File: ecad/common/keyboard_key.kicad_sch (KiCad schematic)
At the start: 3 parts, among them SW2 SW_Push

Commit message: [WIP] Layouting a matric led driver
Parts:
- D2: renamed from D; footprint (none) -> woodpecker:LED_Inolux_IN-PI32TRRRGB_PLCC4_3.2x2.8mm_P1.5mm; MPN (none) -> IN-P32TRRRGB
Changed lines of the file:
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@@
 		(dnp no)
 		(fields_autoplaced yes)
-		(property "Reference" "D"
+		(property "Reference" "D2"
 			(at 109.22 59.6899 90)
 			(effects
@@
 			)
 		)
-		(property "Footprint" ""
+		(property "Footprint" "woodpecker:LED_Inolux_IN-PI32TRRRGB_PLCC4_3.2x2.8mm_P1.5mm"
 			(at 101.6 60.96 0)
 			(effects
@@
 		(property "Description" "RGB LED, blue/green/red/anode"
 			(at 100.33 60.96 0)
+			(effects
+				(font
+					(size 1.27 1.27)
+				)
+				(hide yes)
+			)
+		)
+		(property "MPN" "IN-P32TRRRGB"
+			(at 100.33 60.96 90)
 			(effects
 				(font
@@
 			(project "top_section"
 				(path "/908c4fb0-9cf3-4739-9176-bc5c47ef8a7b/3e4c3c5e-0959-4abd-bf8c-f1b783d7e681"
-					(reference "D18")
+					(reference "D19")
 					(unit 1)
 				)
 				(path "/908c4fb0-9cf3-4739-9176-bc5c47ef8a7b/47cfd13d-bf73-4a03-a6ca-7b66fdb5bb7d"
-					(reference "D12")
+					(reference "D13")
+					(unit 1)
+				)
+				(path "/908c4fb0-9cf3-4739-9176-bc5c47ef8a7b/61fbcd7b-b588-48a7-b7d7-7589f646c796"
+					(reference "D2")
 					(unit 1)
 				)
 				(path "/908c4fb0-9cf3-4739-9176-bc5c47ef8a7b/6c386fc9-dbbe-48da-a0ca-97d6098257c4"
-					(reference "D20")
+					(reference "D21")
 					(unit 1)
 				)
 				(path "/908c4fb0-9cf3-4739-9176-bc5c47ef8a7b/6c8e40cf-9126-4984-9b5c-e41719a9c800"
-					(reference "D10")
+					(reference "D11")
 					(unit 1)
 				)
 				(path "/908c4fb0-9cf3-4739-9176-bc5c47ef8a7b/72a62481-ec11-41eb-95a3-ab230221a7af"
-					(reference "D22")
+					(reference "D23")
 					(unit 1)
 				)
 				(path "/908c4fb0-9cf3-4739-9176-bc5c47ef8a7b/7f0d18ff-a6af-4cf0-a91c-779951147286"
-					(reference "D24")
+					(reference "D25")
 					(unit 1)
 				)
 				(path "/908c4fb0-9cf3-4739-9176-bc5c47ef8a7b/935564e7-05e7-459d-8b7a-ca61f7462e6f"
-					(reference "D16")
+					(reference "D17")
 					(unit 1)
 				)
 				(path "/908c4fb0-9cf3-4739-9176-bc5c47ef8a7b/b7e74592-5a83-4609-924c-57c795101512"
-					(reference "D14")
+					(reference "D15")
 					(unit 1)
 				)
 				(path "/908c4fb0-9cf3-4739-9176-bc5c47ef8a7b/d85b7b05-f8ab-4186-bcfd-5df52ba17141"
-					(reference "D8")
+					(reference "D9")
 					(unit 1)
 				)
@@
 			(project "top_section"
 				(path "/908c4fb0-9cf3-4739-9176-bc5c47ef8a7b/3e4c3c5e-0959-4abd-bf8c-f1b783d7e681"
-					(reference "D19")
+					(reference "D20")
 					(unit 1)
 				)
 				(path "/908c4fb0-9cf3-4739-9176-bc5c47ef8a7b/47cfd13d-bf73-4a03-a6ca-7b66fdb5bb7d"
-					(reference "D13")
+					(reference "D14")
 					(unit 1)
 				)
@@
 				)
 				(path "/908c4fb0-9cf3-4739-9176-bc5c47ef8a7b/6c386fc9-dbbe-48da-a0ca-97d6098257c4"
-					(reference "D21")
+					(reference "D22")
 					(unit 1)
 				)
 				(path "/908c4fb0-9cf3-4739-9176-bc5c47ef8a7b/6c8e40cf-9126-4984-9b5c-e41719a9c800"
-					(reference "D11")
+					(reference "D12")
 					(unit 1)
 				)
 				(path "/908c4fb0-9cf3-4739-9176-bc5c47ef8a7b/72a62481-ec11-41eb-95a3-ab230221a7af"
-					(reference "D23")
+					(reference "D24")
 					(unit 1)
 				)
 				(path "/908c4fb0-9cf3-4739-9176-bc5c47ef8a7b/7f0d18ff-a6af-4cf0-a91c-779951147286"
-					(reference "D25")
+					(reference "D26")
 					(unit 1)
 				)
 				(path "/908c4fb0-9cf3-4739-9176-bc5c47ef8a7b/935564e7-05e7-459d-8b7a-ca61f7462e6f"
-					(reference "D17")
+					(reference "D18")
 					(unit 1)
 				)
 				(path "/908c4fb0-9cf3-4739-9176-bc5c47ef8a7b/b7e74592-5a83-4609-924c-57c795101512"
-					(reference "D15")
+					(reference "D16")
 					(unit 1)
 				)
 				(path "/908c4fb0-9cf3-4739-9176-bc5c47ef8a7b/d85b7b05-f8ab-4186-bcfd-5df52ba17141"
-					(reference "D9")
-					(unit 1)
-				)
+					(reference "D10")
+					(unit 1)
+				)

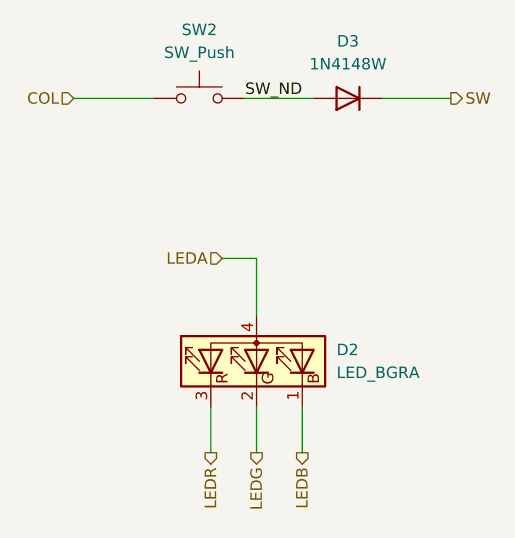
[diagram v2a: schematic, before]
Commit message: Uses LED Matrix controller on all board.
It simplifies so much the design for a small cost.
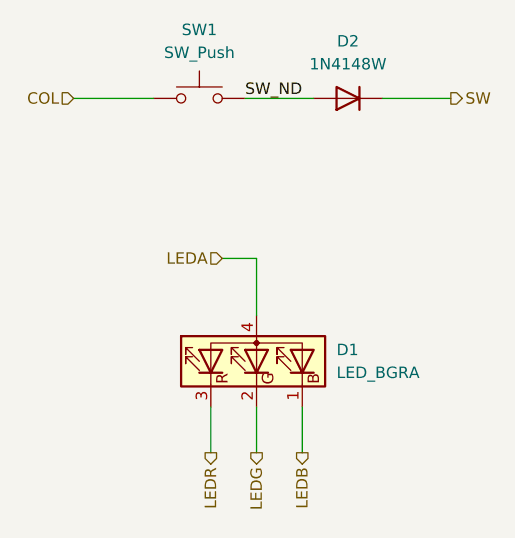
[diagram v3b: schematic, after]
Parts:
- renumbered D2 to D1, D3 to D2, SW2 to SW1
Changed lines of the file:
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@@
 		(on_board yes)
 		(dnp no)
-		(property "Reference" "SW2"
+		(property "Reference" "SW1"
 			(at 93.98 24.13 0)
 			(effects
@@
 		)
 		(instances
-			(project "top_section"
-				(path "/908c4fb0-9cf3-4739-9176-bc5c47ef8a7b/3e4c3c5e-0959-4abd-bf8c-f1b783d7e681"
-					(reference "SW13")
-					(unit 1)
-				)
-				(path "/908c4fb0-9cf3-4739-9176-bc5c47ef8a7b/47cfd13d-bf73-4a03-a6ca-7b66fdb5bb7d"
+			(project "bottom_section"
+				(path "/e5586514-98d8-4785-a096-88fc3a51b1f3/1d252128-5a15-4d61-935a-3deb595aa18f"
+					(reference "SW5")
+					(unit 1)
+				)
+				(path "/e5586514-98d8-4785-a096-88fc3a51b1f3/4e0f2a1f-84c1-4159-b51f-b8ab8493fd2c"
+					(reference "SW6")
+					(unit 1)
+				)
+				(path "/e5586514-98d8-4785-a096-88fc3a51b1f3/5978120e-7110-4ebf-b594-4881798784db"
 					(reference "SW10")
 					(unit 1)
 				)
-				(path "/908c4fb0-9cf3-4739-9176-bc5c47ef8a7b/61fbcd7b-b588-48a7-b7d7-7589f646c796"
+				(path "/e5586514-98d8-4785-a096-88fc3a51b1f3/61a04379-d684-4de2-8564-18b65f6be942"
+					(reference "SW7")
+					(unit 1)
+				)
+				(path "/e5586514-98d8-4785-a096-88fc3a51b1f3/972bcb43-2c03-4a62-ab04-b4b2649c149d"
+					(reference "SW4")
+					(unit 1)
+				)
+				(path "/e5586514-98d8-4785-a096-88fc3a51b1f3/a60112cb-2a25-4cee-b7dc-a72ac75dbb95"
+					(reference "SW9")
+					(unit 1)
+				)
+				(path "/e5586514-98d8-4785-a096-88fc3a51b1f3/b05b7d89-e8e3-4430-b508-1898dbbdfc32"
+					(reference "SW1")
+					(unit 1)
+				)
+				(path "/e5586514-98d8-4785-a096-88fc3a51b1f3/e33e4fdc-bd58-4c67-bb99-1ce8e87238a8"
 					(reference "SW2")
 					(unit 1)
 				)
-				(path "/908c4fb0-9cf3-4739-9176-bc5c47ef8a7b/6c386fc9-dbbe-48da-a0ca-97d6098257c4"
-					(reference "SW14")
-					(unit 1)
-				)
-				(path "/908c4fb0-9cf3-4739-9176-bc5c47ef8a7b/6c8e40cf-9126-4984-9b5c-e41719a9c800"
-					(reference "SW9")
-					(unit 1)
-				)
-				(path "/908c4fb0-9cf3-4739-9176-bc5c47ef8a7b/72a62481-ec11-41eb-95a3-ab230221a7af"
-					(reference "SW15")
-					(unit 1)
-				)
-				(path "/908c4fb0-9cf3-4739-9176-bc5c47ef8a7b/7f0d18ff-a6af-4cf0-a91c-779951147286"
-					(reference "SW16")
-					(unit 1)
-				)
-				(path "/908c4fb0-9cf3-4739-9176-bc5c47ef8a7b/935564e7-05e7-459d-8b7a-ca61f7462e6f"
-					(reference "SW12")
-					(unit 1)
-				)
-				(path "/908c4fb0-9cf3-4739-9176-bc5c47ef8a7b/b7e74592-5a83-4609-924c-57c795101512"
-					(reference "SW11")
-					(unit 1)
-				)
-				(path "/908c4fb0-9cf3-4739-9176-bc5c47ef8a7b/d85b7b05-f8ab-4186-bcfd-5df52ba17141"
+				(path "/e5586514-98d8-4785-a096-88fc3a51b1f3/e46df20f-6acd-4ec4-b154-0a8435b82625"
 					(reference "SW8")
+					(unit 1)
+				)
+				(path "/e5586514-98d8-4785-a096-88fc3a51b1f3/fe8acc3a-547c-469d-9f32-08486ec377e4"
+					(reference "SW3")
 					(unit 1)
 				)
@@
 		(dnp no)
 		(fields_autoplaced yes)
-		(property "Reference" "D2"
+		(property "Reference" "D1"
 			(at 109.22 59.6899 90)
 			(effects
@@
 		)
 		(instances
-			(project "top_section"
-				(path "/908c4fb0-9cf3-4739-9176-bc5c47ef8a7b/3e4c3c5e-0959-4abd-bf8c-f1b783d7e681"
+			(project "bottom_section"
+				(path "/e5586514-98d8-4785-a096-88fc3a51b1f3/1d252128-5a15-4d61-935a-3deb595aa18f"
+					(reference "D9")
+					(unit 1)
+				)
+				(path "/e5586514-98d8-4785-a096-88fc3a51b1f3/4e0f2a1f-84c1-4159-b51f-b8ab8493fd2c"
+					(reference "D11")
+					(unit 1)
+				)
+				(path "/e5586514-98d8-4785-a096-88fc3a51b1f3/5978120e-7110-4ebf-b594-4881798784db"
 					(reference "D19")
 					(unit 1)
 				)
-				(path "/908c4fb0-9cf3-4739-9176-bc5c47ef8a7b/47cfd13d-bf73-4a03-a6ca-7b66fdb5bb7d"
+				(path "/e5586514-98d8-4785-a096-88fc3a51b1f3/61a04379-d684-4de2-8564-18b65f6be942"
 					(reference "D13")
 					(unit 1)
 				)
-				(path "/908c4fb0-9cf3-4739-9176-bc5c47ef8a7b/61fbcd7b-b588-48a7-b7d7-7589f646c796"
-					(reference "D2")
-					(unit 1)
-				)
-				(path "/908c4fb0-9cf3-4739-9176-bc5c47ef8a7b/6c386fc9-dbbe-48da-a0ca-97d6098257c4"
-					(reference "D21")
-					(unit 1)
-				)
-				(path "/908c4fb0-9cf3-4739-9176-bc5c47ef8a7b/6c8e40cf-9126-4984-9b5c-e41719a9c800"
-					(reference "D11")
-					(unit 1)
-				)
-				(path "/908c4fb0-9cf3-4739-9176-bc5c47ef8a7b/72a62481-ec11-41eb-95a3-ab230221a7af"
-					(reference "D23")
-					(unit 1)
-				)
-				(path "/908c4fb0-9cf3-4739-9176-bc5c47ef8a7b/7f0d18ff-a6af-4cf0-a91c-779951147286"
-					(reference "D25")
-					(unit 1)
-				)
-				(path "/908c4fb0-9cf3-4739-9176-bc5c47ef8a7b/935564e7-05e7-459d-8b7a-ca61f7462e6f"
+				(path "/e5586514-98d8-4785-a096-88fc3a51b1f3/972bcb43-2c03-4a62-ab04-b4b2649c149d"
+					(reference "D7")
+					(unit 1)
+				)
+				(path "/e5586514-98d8-4785-a096-88fc3a51b1f3/a60112cb-2a25-4cee-b7dc-a72ac75dbb95"
 					(reference "D17")
 					(unit 1)
 				)
-				(path "/908c4fb0-9cf3-4739-9176-bc5c47ef8a7b/b7e74592-5a83-4609-924c-57c795101512"
+				(path "/e5586514-98d8-4785-a096-88fc3a51b1f3/b05b7d89-e8e3-4430-b508-1898dbbdfc32"
+					(reference "D1")
+					(unit 1)
+				)
+				(path "/e5586514-98d8-4785-a096-88fc3a51b1f3/e33e4fdc-bd58-4c67-bb99-1ce8e87238a8"
+					(reference "D3")
+					(unit 1)
+				)
+				(path "/e5586514-98d8-4785-a096-88fc3a51b1f3/e46df20f-6acd-4ec4-b154-0a8435b82625"
 					(reference "D15")
 					(unit 1)
 				)
-				(path "/908c4fb0-9cf3-4739-9176-bc5c47ef8a7b/d85b7b05-f8ab-4186-bcfd-5df52ba17141"
-					(reference "D9")
+				(path "/e5586514-98d8-4785-a096-88fc3a51b1f3/fe8acc3a-547c-469d-9f32-08486ec377e4"
+					(reference "D5")
 					(unit 1)
 				)
@@
 		(dnp no)
 		(fields_autoplaced yes)
-		(property "Reference" "D3"
+		(property "Reference" "D2"
 			(at 110.49 25.4 0)
 			(effects
@@
 		)
 		(instances
-			(project "top_section"
-				(path "/908c4fb0-9cf3-4739-9176-bc5c47ef8a7b/3e4c3c5e-0959-4abd-bf8c-f1b783d7e681"
+			(project "bottom_section"
+				(path "/e5586514-98d8-4785-a096-88fc3a51b1f3/1d252128-5a15-4d61-935a-3deb595aa18f"
+					(reference "D10")
+					(unit 1)
+				)
+				(path "/e5586514-98d8-4785-a096-88fc3a51b1f3/4e0f2a1f-84c1-4159-b51f-b8ab8493fd2c"
+					(reference "D12")
+					(unit 1)
+				)
+				(path "/e5586514-98d8-4785-a096-88fc3a51b1f3/5978120e-7110-4ebf-b594-4881798784db"
 					(reference "D20")
 					(unit 1)
 				)
-				(path "/908c4fb0-9cf3-4739-9176-bc5c47ef8a7b/47cfd13d-bf73-4a03-a6ca-7b66fdb5bb7d"
+				(path "/e5586514-98d8-4785-a096-88fc3a51b1f3/61a04379-d684-4de2-8564-18b65f6be942"
 					(reference "D14")
 					(unit 1)
 				)
-				(path "/908c4fb0-9cf3-4739-9176-bc5c47ef8a7b/61fbcd7b-b588-48a7-b7d7-7589f646c796"
-					(reference "D3")
-					(unit 1)
-				)
-				(path "/908c4fb0-9cf3-4739-9176-bc5c47ef8a7b/6c386fc9-dbbe-48da-a0ca-97d6098257c4"
-					(reference "D22")
-					(unit 1)
-				)
-				(path "/908c4fb0-9cf3-4739-9176-bc5c47ef8a7b/6c8e40cf-9126-4984-9b5c-e41719a9c800"
-					(reference "D12")
-					(unit 1)
-				)
-				(path "/908c4fb0-9cf3-4739-9176-bc5c47ef8a7b/72a62481-ec11-41eb-95a3-ab230221a7af"
-					(reference "D24")
-					(unit 1)
-				)
-				(path "/908c4fb0-9cf3-4739-9176-bc5c47ef8a7b/7f0d18ff-a6af-4cf0-a91c-779951147286"
-					(reference "D26")
-					(unit 1)
-				)
-				(path "/908c4fb0-9cf3-4739-9176-bc5c47ef8a7b/935564e7-05e7-459d-8b7a-ca61f7462e6f"
+				(path "/e5586514-98d8-4785-a096-88fc3a51b1f3/972bcb43-2c03-4a62-ab04-b4b2649c149d"
+					(reference "D8")
+					(unit 1)
+				)
+				(path "/e5586514-98d8-4785-a096-88fc3a51b1f3/a60112cb-2a25-4cee-b7dc-a72ac75dbb95"
 					(reference "D18")
 					(unit 1)
 				)
-				(path "/908c4fb0-9cf3-4739-9176-bc5c47ef8a7b/b7e74592-5a83-4609-924c-57c795101512"
+				(path "/e5586514-98d8-4785-a096-88fc3a51b1f3/b05b7d89-e8e3-4430-b508-1898dbbdfc32"
+					(reference "D2")
+					(unit 1)
+				)
+				(path "/e5586514-98d8-4785-a096-88fc3a51b1f3/e33e4fdc-bd58-4c67-bb99-1ce8e87238a8"
+					(reference "D4")
+					(unit 1)
+				)
+				(path "/e5586514-98d8-4785-a096-88fc3a51b1f3/e46df20f-6acd-4ec4-b154-0a8435b82625"
 					(reference "D16")
 					(unit 1)
 				)
-				(path "/908c4fb0-9cf3-4739-9176-bc5c47ef8a7b/d85b7b05-f8ab-4186-bcfd-5df52ba17141"
-					(reference "D10")
-					(unit 1)
-				)
+				(path "/e5586514-98d8-4785-a096-88fc3a51b1f3/fe8acc3a-547c-469d-9f32-08486ec377e4"
+					(reference "D6")
+					(unit 1)
+				)

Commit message: First production run for PCB
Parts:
- D3: renamed from D2; MPN (none) -> 1N4148W
- SW2: renamed from SW1; MPN (none) -> 1528-5118-ND
- renumbered D1 to D2
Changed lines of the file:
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@@
 		(on_board yes)
 		(dnp no)
-		(property "Reference" "SW1"
+		(property "Reference" "SW2"
 			(at 93.98 24.13 0)
 			(effects
@@
 		)
 		(property "Manufacturer" ""
+			(at 93.98 31.75 0)
+			(effects
+				(font
+					(size 1.27 1.27)
+				)
+				(hide yes)
+			)
+		)
+		(property "MPN" "1528-5118-ND"
 			(at 93.98 31.75 0)
 			(effects
@@
 		(dnp no)
 		(fields_autoplaced yes)
-		(property "Reference" "D1"
+		(property "Reference" "D2"
 			(at 109.22 59.6899 90)
 			(effects
@@
 		(dnp no)
 		(fields_autoplaced yes)
-		(property "Reference" "D2"
+		(property "Reference" "D3"
 			(at 110.49 25.4 0)
 			(effects
@@
 			(at 110.49 31.75 0)
 			(effects
+				(font
+					(size 1.27 1.27)
+				)
+				(hide yes)
+			)
+		)
+		(property "MPN" "1N4148W"
+			(at 110.49 31.75 0)
+			(effects

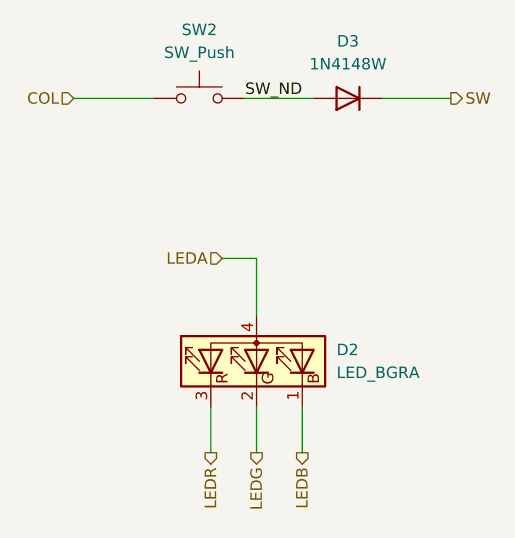
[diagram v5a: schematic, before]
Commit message: Outputs new  step files
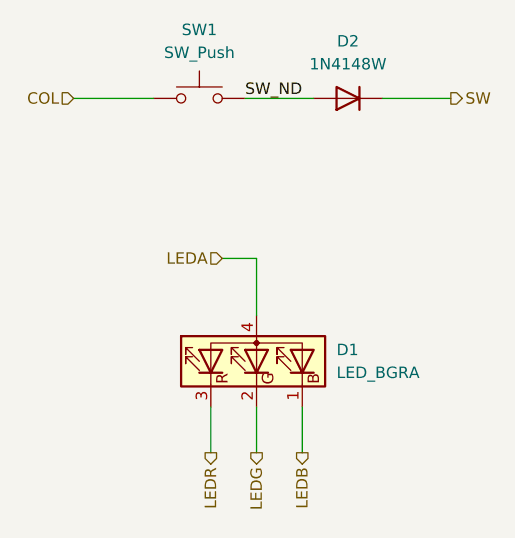
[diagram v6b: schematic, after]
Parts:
- renumbered D2 to D1, D3 to D2, SW2 to SW1
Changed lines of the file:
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@@
 		(on_board yes)
 		(dnp no)
-		(property "Reference" "SW2"
+		(property "Reference" "SW1"
 			(at 93.98 24.13 0)
 			(effects
@@
 		(dnp no)
 		(fields_autoplaced yes)
-		(property "Reference" "D2"
+		(property "Reference" "D1"
 			(at 109.22 59.6899 90)
 			(effects
@@
 		(dnp no)
 		(fields_autoplaced yes)
-		(property "Reference" "D3"
+		(property "Reference" "D2"
 			(at 110.49 25.4 0)
 			(effects
